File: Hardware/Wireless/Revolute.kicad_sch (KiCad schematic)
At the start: 55 parts, among them U1 BQ27441-G1, U2 Button, U2 nrf52833_qfn40, U3 AS5600, U4 AP2112K-3.3, U5 BQ24075RGT, X1 32.768 kHz, X2 32MHZ

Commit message: modified wireless PCB
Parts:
- U3: footprint Package_SO:SOIC-8-1EP_3.9x4.9mm_P1.27mm_EP2.514x3.2mm -> Library:SOIC-8-1EP_3.9x4.9mm_P1.27mm_EP2.514x3.2mm
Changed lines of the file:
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@@
 		(dnp no)
 		(property "Reference" "U41"
-			(at 130.81 159.385 0)
+			(at 130.048 160.274 0)
 			(effects
 				(font
@@
 			)
 		)
-		(property "Footprint" "Package_SO:SOIC-8-1EP_3.9x4.9mm_P1.27mm_EP2.514x3.2mm"
+		(property "Footprint" "Library:SOIC-8-1EP_3.9x4.9mm_P1.27mm_EP2.514x3.2mm"
 			(at 170.18 98.425 0)
 			(effects

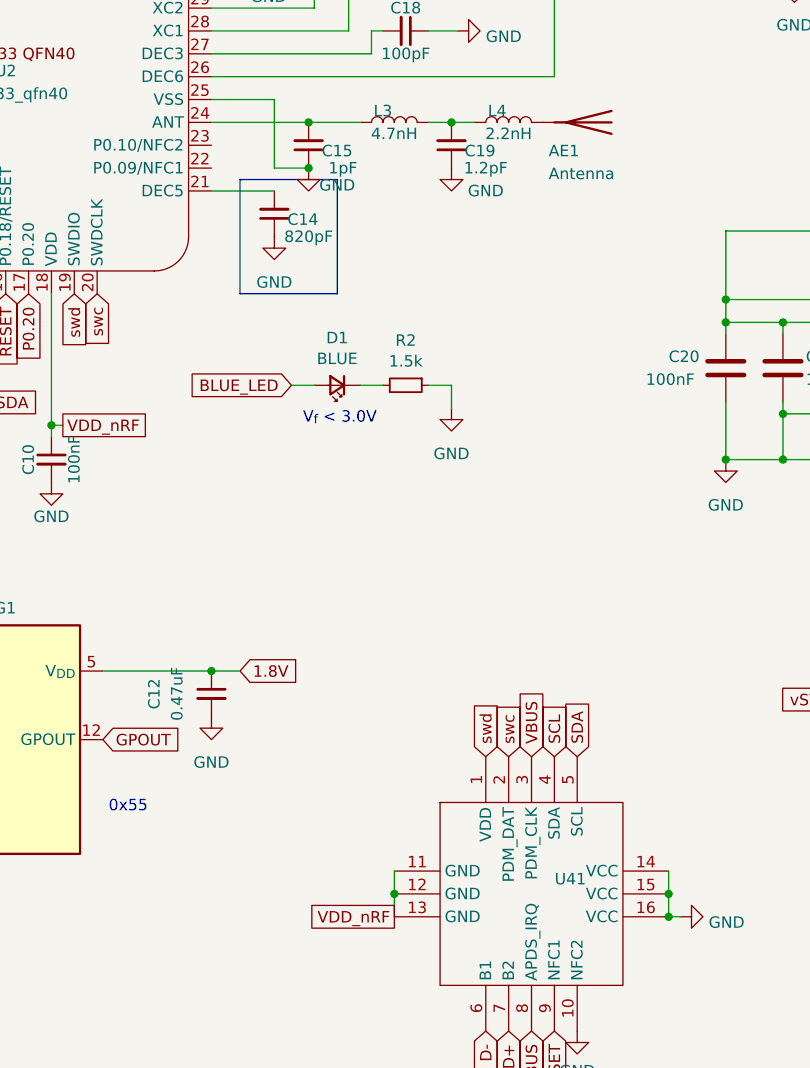
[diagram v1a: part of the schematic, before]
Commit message: added ID column
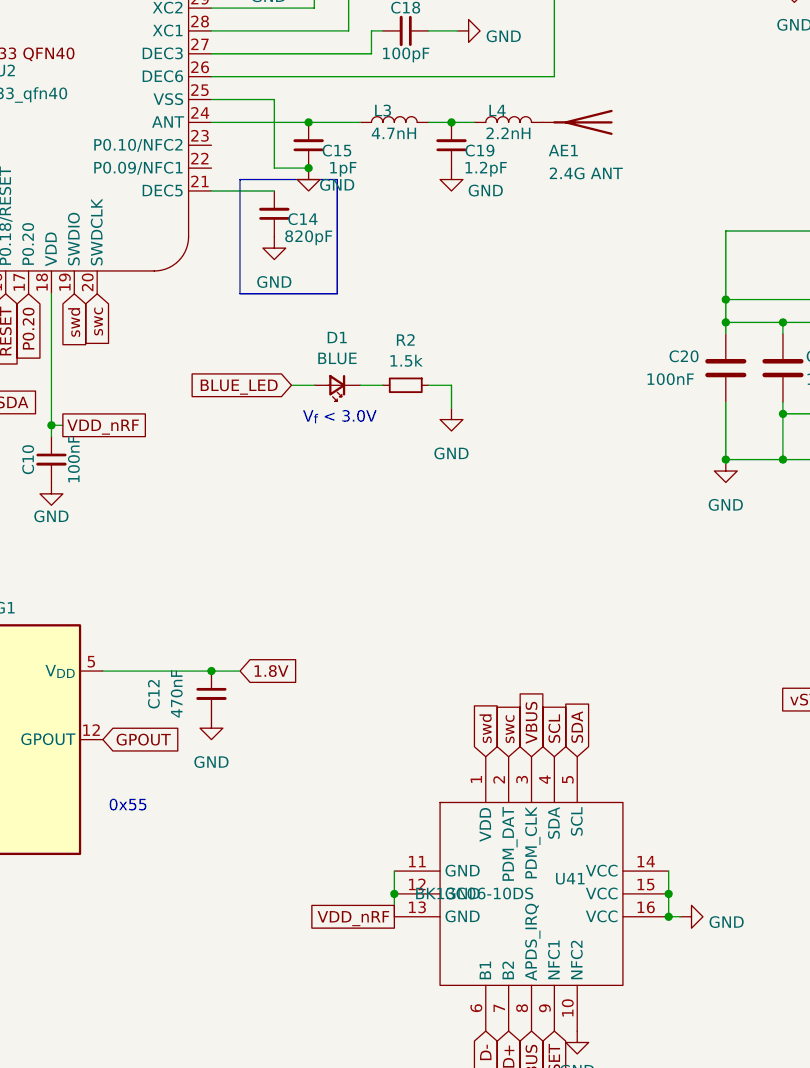
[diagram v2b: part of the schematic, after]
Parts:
- AE1: value Antenna -> 2.4G ANT; ID (none) -> 106
- C1, C6, C8: ID (none) -> 16
- C10, C13, C20, C5: ID (none) -> 21
- C11: ID (none) -> 55
- C12: value 0.47uF -> 470nF; ID (none) -> 12
- C14: ID (none) -> 26
- C15: ID (none) -> 18
- C16, C17, C2, C3: ID (none) -> 17
- C18: ID (none) -> 56
- C19: ID (none) -> 112
- C21, C22, C23, C24, C4, C7, C9: ID (none) -> 30
- C25, C26: ID (none) -> 83
- D1: ID (none) -> 90; JLC Part C72041 -> (none); LCSC Part C146215 -> (none); Manufacturer Part 19-217/BHC-ZL1M2RY/3T -> (none)
- D2: ID (none) -> 97
- L1: ID (none) -> 57
- L2: ID (none) -> 11
- L3: ID (none) -> 104
- L4: ID (none) -> 101
- R1: ID (none) -> 110
- R2: ID (none) -> 27
- R3: ID (none) -> 6
- R4: ID (none) -> 105; JLC Part C25867 -> (none); LCSC Part C114759 -> (none); Manufacturer Part RC0402FR-071K5L -> (none)
- R5: ID (none) -> 77; JLC Part C25867 -> (none); LCSC Part C114759 -> (none); Manufacturer Part RC0402FR-071K5L -> (none)
- R6, R8: ID (none) -> 29
- R7: ID (none) -> 7; JLC Part C25867 -> (none); LCSC Part C114759 -> (none); Manufacturer Part RC0402FR-071K5L -> (none)
- R9: ID (none) -> 82; JLC Part C25867 -> (none); LCSC Part C114759 -> (none); Manufacturer Part RC0402FR-071K5L -> (none)
- TH1: ID (none) -> 31
- U1: ID (none) -> 92
- U2: ID (none) -> 107
- U3: ID (none) -> 73
- U4: ID (none) -> 62
- U41: value ~ -> BK13C06-10DS; ID (none) -> 41
- U5: ID (none) -> 93
- X1: Digikey 728-1075-1-ND -> (none); ID (none) -> 43; JLC Part C93231 -> (none); LCSC Part C97607 -> (none); Manufacturer Part SC20S-12.5PF20PPM -> (none)
- X2: ID (none) -> 42

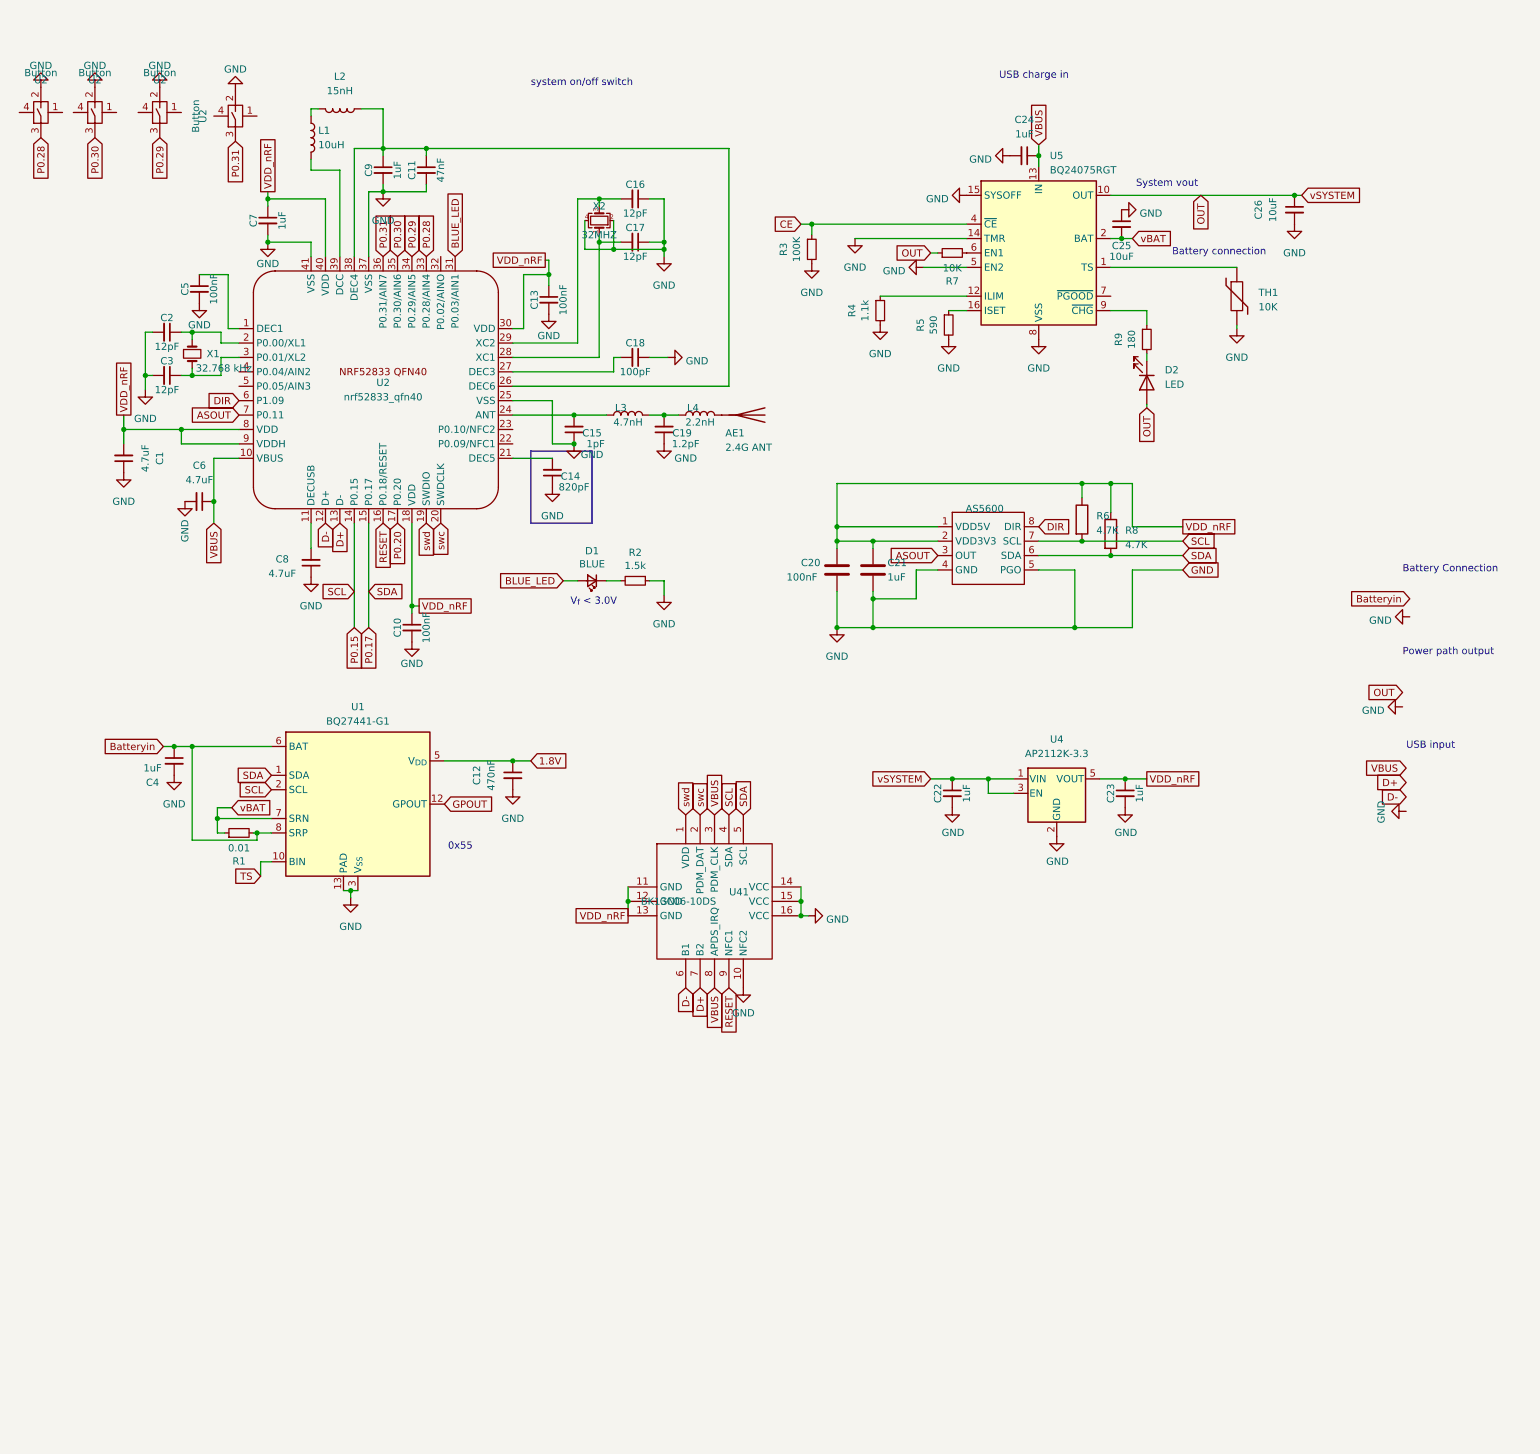
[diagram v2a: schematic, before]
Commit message: migrated components to 0201
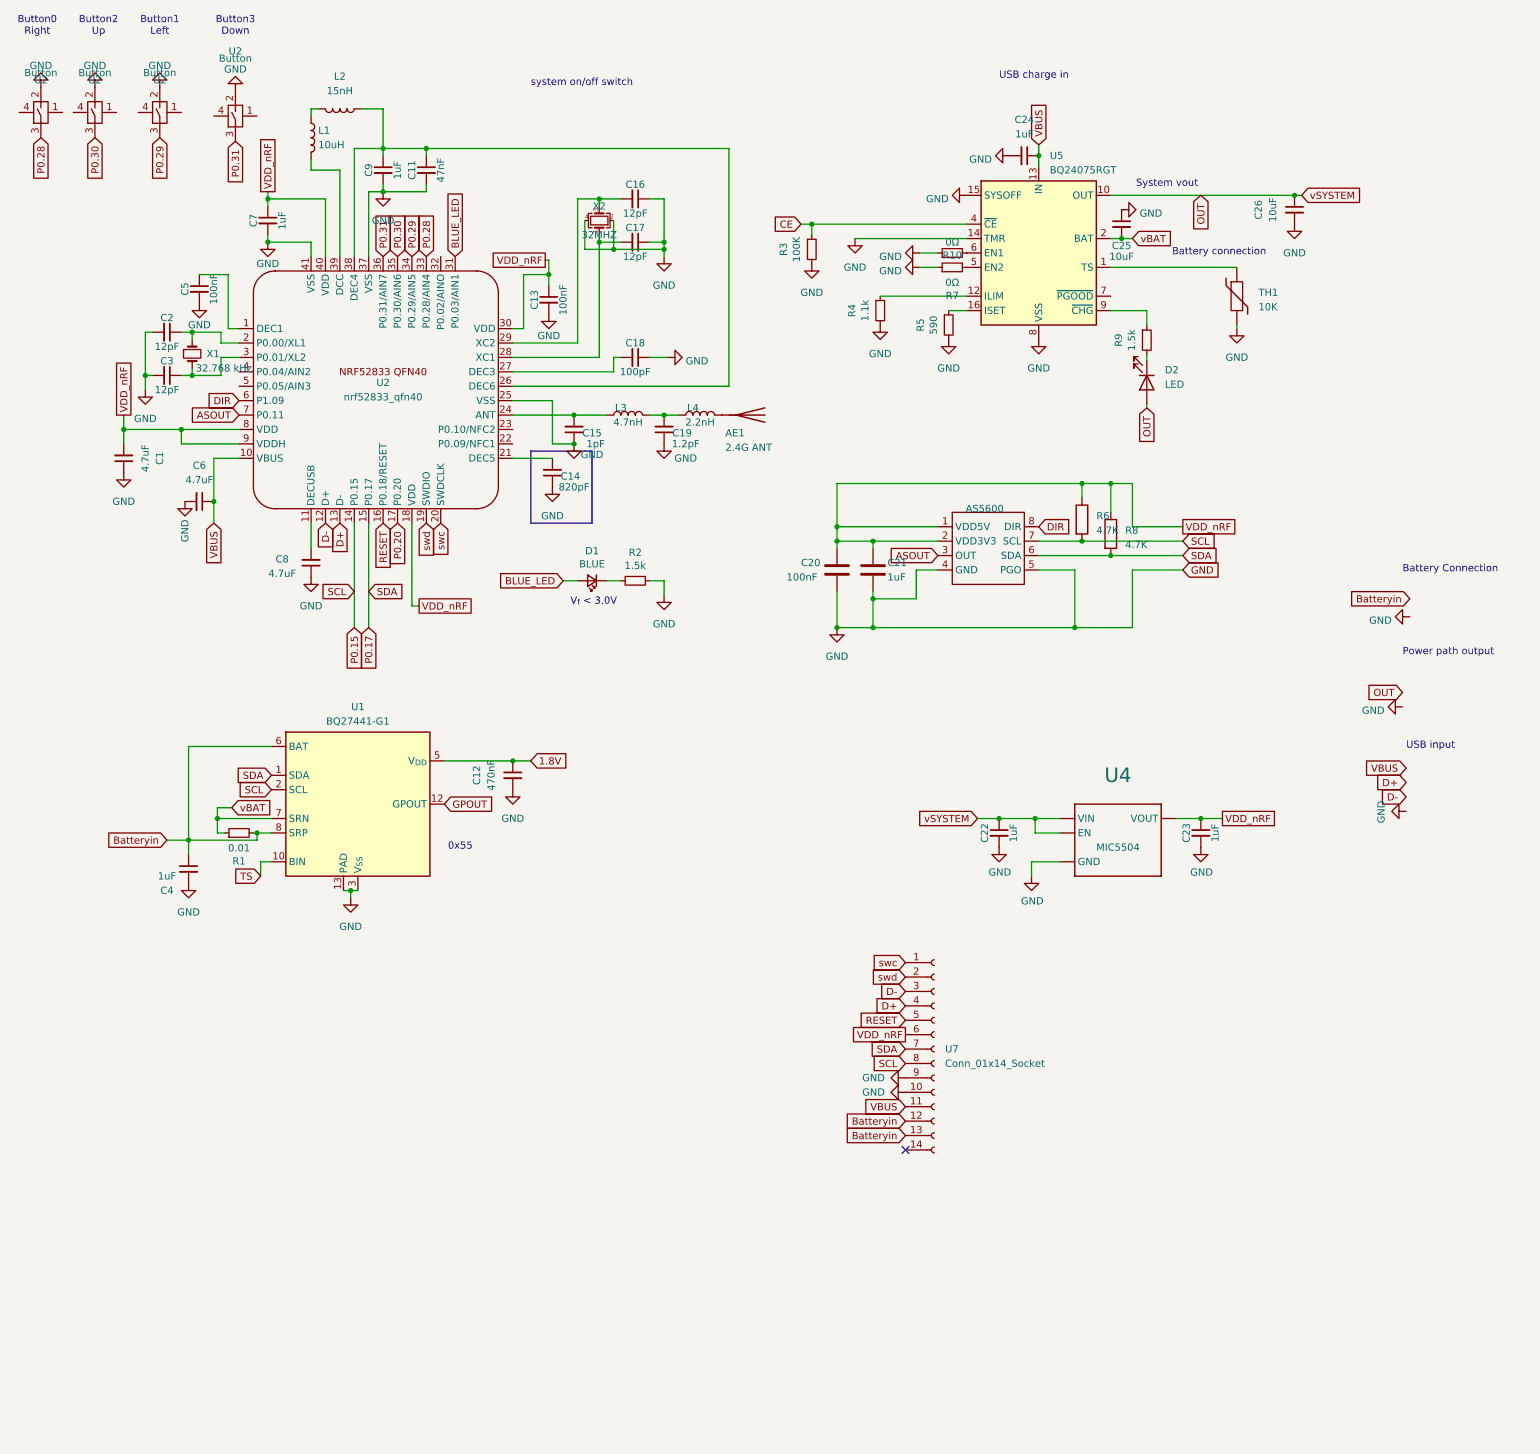
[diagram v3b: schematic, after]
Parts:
- removed C10: 100nF, Capacitor_SMD:C_0402_1005Metric, symbol Device:C_Small
- removed U4: AP2112K-3.3, Package_TO_SOT_SMD:SOT-23-5, symbol Regulator_Linear:AP2112K-3.3
- removed U41: BK13C06-10DS, Library:BK13C06-10DS, symbol Library:BK13C06-10D(S/P)
- added R10: 0Ω, Library:Resistor-0201, symbol Device:R_Small
- added U4: MIC5504, Library:TDFN-4, symbol ESP32-eagle-import:MIC5504
- added U7: Conn_01x14_Socket, Library:FPC, symbol Connector:Conn_01x14_Socket
- C1, C11, C12, C13, C14, C16, C17, C18, C2, C20, C21, C22, C23, C24, C3, C4, C5, C6, C7, C8, C9: footprint Capacitor_SMD:C_0402_1005Metric -> Library:Capacitor-0201
- R3: footprint Library:Resistor_0402_1005M-nosilk -> Library:Resistor-0201
- R6, R8: footprint Resistor_SMD:R_0402_1005Metric -> Library:Resistor-0201
- R7: value 10K -> 0Ω; footprint Library:Resistor_0402_1005M-nosilk -> Library:Resistor-0201; ID 7 -> 10
- R9: value 180 -> 1.5k; footprint Library:Resistor_0402_1005M-nosilk -> Library:Resistor-0201; ID 82 -> 27; JLC Part (none) -> C25867; LCSC Part (none) -> C114759; Manufacturer Part (none) -> RC0402FR-071K5L
- U2: ID (none) -> 116
- X2: footprint Library:crystal 32mhz -> Library:Crystal_SMD_2016-4Pin_2.0x1.6mm
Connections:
- net Batteryin: now also U7.12 (Pin_12), U7.13 (Pin_13)
- net D+: now also U7.4 (Pin_4)
- net D-: now also U7.3 (Pin_3)
- net GND: now also R7.1, R10.1, U4.2 (GND), U4.5 (GND), U7.10 (Pin_10), U7.9 (Pin_9); no longer U5.5 (EN2)
- net OUT: now also U4.3 (EN), U4.4 (VIN); no longer R7.1
- net P0.15: now also U7.8 (Pin_8)
- net P0.17: now also U7.7 (Pin_7)
- net RESET: now also U7.5 (Pin_5)
- net VBUS: now also U7.11 (Pin_11)
- net VDD_nRF: now also U4.1 (VOUT), U7.6 (Pin_6)
- net swc: now also U7.1 (Pin_1)
- net swd: now also U7.2 (Pin_2)
- net at U5.6 (EN1): now also R10.2; no longer R7.2
- new net: R7.2, U5.5 (EN2)
- no-connect marks 0 -> 1
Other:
- note added: "Button0 Right"
- note added: "Button1 Left"
- note added: "Button2 Up"
- note added: "Button3 Down"
- moved on the sheet: C22, C23, C4, R7

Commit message: current version
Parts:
- AE1: footprint RF_Antenna:Johanson_2450AT18x100 -> Library:Antenna 2450AT42A100
- C1, C6, C8: ID 16 -> 140
- C11: ID 55 -> 139
- C13, C20, C5: ID 21 -> 145
- C14: ID 26 -> 137
- C15: footprint Capacitor_SMD:C_0402_1005Metric -> Library:Capacitor-0201; ID 18 -> 146
- C16, C17, C2, C3: ID 17 -> 142
- C18: ID 56 -> 141
- C19: footprint Capacitor_SMD:C_0402_1005Metric -> Library:Capacitor-0201; ID 112 -> 144
- C21, C22, C23, C24, C4, C7, C9: ID 30 -> 136
- R1: JLC Part C25867 -> (none); LCSC Part C114759 -> (none); Manufacturer Part RC0402FR-071K5L -> (none)
- R2: footprint Library:Resistor_0402_1005M-nosilk -> Library:Resistor-0201; ID 27 -> 138; JLC Part C25867 -> (none); LCSC Part C114759 -> (none); Manufacturer Part RC0402FR-071K5L -> (none)
- R3: ID 6 -> 131; JLC Part C25867 -> (none); LCSC Part C114759 -> (none); Manufacturer Part RC0402FR-071K5L -> (none)
- R6, R8: ID 29 -> 135
- R9: ID 27 -> 138; JLC Part C25867 -> (none); LCSC Part C114759 -> (none); Manufacturer Part RC0402FR-071K5L -> (none)
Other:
- moved on the sheet: U7
